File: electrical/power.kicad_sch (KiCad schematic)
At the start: 46 parts

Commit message: Added overview
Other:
- moved on the sheet: GTR20_CB
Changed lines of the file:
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@@
     (title "Power Distribution")
     (date "2024-02-12")
-    (rev "0.5")
+    (rev "0.9")
     (company "N877RV")
   )
@@
   (junction (at 127 40.64) (diameter 0) (color 0 0 0 0)
   )
-  (junction (at 175.26 137.16) (diameter 0) (color 0 0 0 0)
+  (junction (at 157.48 137.16) (diameter 0) (color 0 0 0 0)
   )
   (junction (at 123.19 222.25) (diameter 0) (color 0 0 0 0)
@@
     (stroke (width 0) (type default))
   )
-  (bus_entry (at 152.4 134.62) (size 2.54 2.54)
+  (bus_entry (at 134.62 134.62) (size 2.54 2.54)
     (stroke (width 0) (type default))
   )
@@
     (stroke (width 0) (type default))
   )
-  (wire (pts (xy 175.26 140.97) (xy 175.26 137.16))
+  (wire (pts (xy 157.48 140.97) (xy 157.48 137.16))
     (stroke (width 0) (type default))
   )
@@
     (stroke (width 0) (type default))
   )
-  (bus (pts (xy 134.62 124.46) (xy 134.62 143.51))
+  (bus (pts (xy 134.62 124.46) (xy 134.62 134.62))
+    (stroke (width 0) (type default))
+  )
+  (bus (pts (xy 134.62 134.62) (xy 134.62 143.51))
     (stroke (width 0) (type default))
   )
@@
     (stroke (width 0) (type default))
   )
-  (bus (pts (xy 152.4 127) (xy 152.4 134.62))
-    (stroke (width 0) (type default))
-  )
   (wire (pts (xy 127 60.96) (xy 133.35 60.96))
     (stroke (width 0) (type default))
@@
     (stroke (width 0) (type default))
   )
-  (wire (pts (xy 176.53 140.97) (xy 175.26 140.97))
+  (wire (pts (xy 158.75 140.97) (xy 157.48 140.97))
     (stroke (width 0) (type default))
   )
@@
     (stroke (width 0) (type default))
   )
-  (wire (pts (xy 154.94 137.16) (xy 157.48 137.16))
+  (wire (pts (xy 137.16 137.16) (xy 139.7 137.16))
     (stroke (width 0) (type default))
   )
@@
     (stroke (width 0) (type default))
   )
-  (wire (pts (xy 175.26 137.16) (xy 184.15 137.16))
+  (wire (pts (xy 157.48 137.16) (xy 166.37 137.16))
     (stroke (width 0) (type default))
   )
@@
     (effects (font (size 1.27 1.27)) (justify left))
   )
-  (hierarchical_label "GTR20_PWR" (shape output) (at 184.15 137.16 0) (fields_autoplaced)
+  (hierarchical_label "GTR20_PWR" (shape output) (at 166.37 137.16 0) (fields_autoplaced)
     (effects (font (size 1.27 1.27)) (justify left))
   )
@@
     (effects (font (size 1.27 1.27)) (justify left))
   )
-  (hierarchical_label "LEMO_PWR" (shape output) (at 184.15 140.97 0) (fields_autoplaced)
+  (hierarchical_label "LEMO_PWR" (shape output) (at 166.37 140.97 0) (fields_autoplaced)
     (effects (font (size 1.27 1.27)) (justify left))
   )
@@
     )
   )
-  (symbol (lib_id "Device:Fuse") (at 180.34 140.97 90) (unit 1)
-    (in_bom yes) (on_board yes) (dnp no)
-    (property "Reference" "LEMO_FS1" (at 180.34 137.16 90)
-      (effects (font (size 1.27 1.27)) hide)
-    )
-    (property "Value" "1" (at 180.34 138.43 90)
-      (effects (font (size 1.27 1.27)))
-    )
-    (property "Footprint" "" (at 180.34 142.748 90)
-      (effects (font (size 1.27 1.27)) hide)
-    )
-    (property "Datasheet" "~" (at 180.34 140.97 0)
+  (symbol (lib_id "Device:Fuse") (at 162.56 140.97 90) (unit 1)
+    (in_bom yes) (on_board yes) (dnp no)
+    (property "Reference" "LEMO_FS1" (at 162.56 137.16 90)
+      (effects (font (size 1.27 1.27)) hide)
+    )
+    (property "Value" "1" (at 162.56 138.43 90)
+      (effects (font (size 1.27 1.27)))
+    )
+    (property "Footprint" "" (at 162.56 142.748 90)
+      (effects (font (size 1.27 1.27)) hide)
+    )
+    (property "Datasheet" "~" (at 162.56 140.97 0)
       (effects (font (size 1.27 1.27)) hide)
     )
@@
     )
   )
-  (symbol (lib_id "flyerx:Circuit_Breaker") (at 166.37 134.62 0) (unit 1)
-    (in_bom yes) (on_board yes) (dnp no)
-    (property "Reference" "GTR20_CB" (at 166.37 132.08 0)
-      (effects (font (size 1.27 1.27)))
-    )
-    (property "Value" "3A" (at 166.37 137.16 0)
-      (effects (font (size 1.27 1.27)))
-    )
-    (property "Footprint" "" (at 166.37 134.62 0)
-      (effects (font (size 1.27 1.27)) hide)
-    )
-    (property "Datasheet" "" (at 166.37 134.62 0)
-      (effects (font (size 1.27 1.27)) hide)
-    )
+  (symbol (lib_id "flyerx:Circuit_Breaker") (at 148.59 134.62 0) (unit 1)
+    (in_bom yes) (on_board yes) (dnp no)
+    (property "Reference" "GTR20_CB" (at 148.59 132.08 0)
+      (effects (font (size 1.27 1.27)))
+    )
+    (property "Value" "3A" (at 148.59 137.16 0)
+      (effects (font (size 1.27 1.27)))
+    )
+    (property "Footprint" "" (at 148.59 134.62 0)
+      (effects (font (size 1.27 1.27)) hide)
+    )
+    (property "Datasheet" "" (at 148.59 134.62 0)
+      (effects (font (size 1.27 1.27)) hide)
+    )

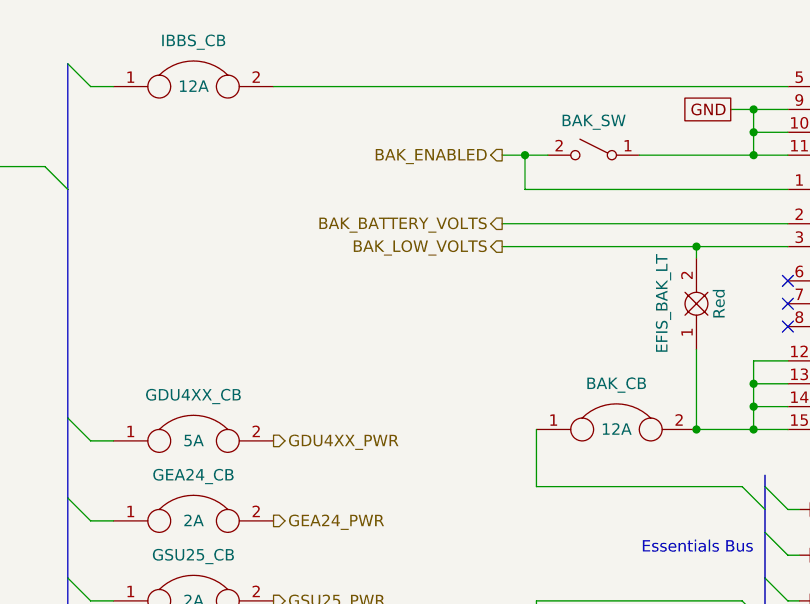
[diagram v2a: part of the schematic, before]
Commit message: Added V speeds to panel. Added note about backup power & circuit breakers. Changed backup battery circuit breaker size.
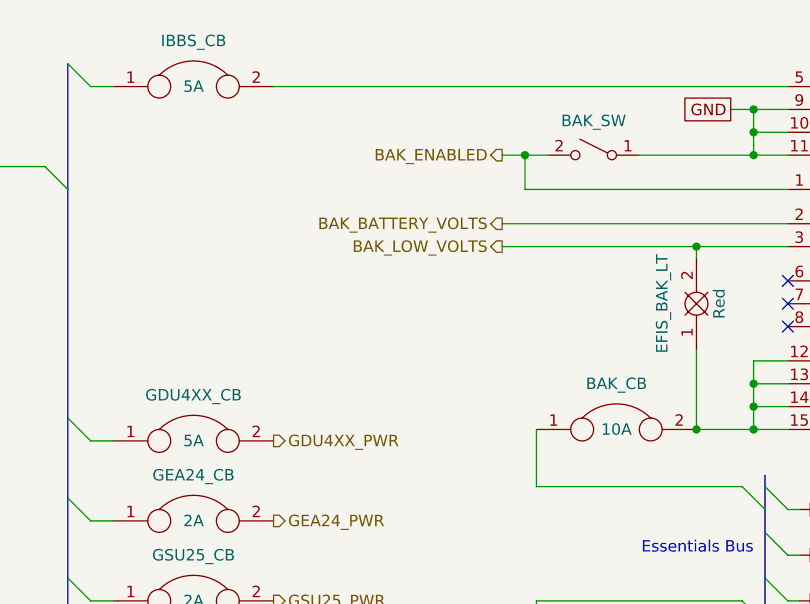
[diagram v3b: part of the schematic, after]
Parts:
- BAK_CB: value 12A -> 10A
- IBBS_CB: value 12A -> 5A
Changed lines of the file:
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@@
       (effects (font (size 1.27 1.27)))
     )
-    (property "Value" "12A" (at 71.12 22.86 0)
+    (property "Value" "5A" (at 71.12 22.86 0)
       (effects (font (size 1.27 1.27)))
     )
@@
       (effects (font (size 1.27 1.27)))
     )
-    (property "Value" "12A" (at 118.11 60.96 0)
-      (effects (font (size 1.27 1.27)))
-    )
+    (property "Value" "10A" (at 118.11 60.96 0)
+      (effects (font (size 1.27 1.27)))
+    )

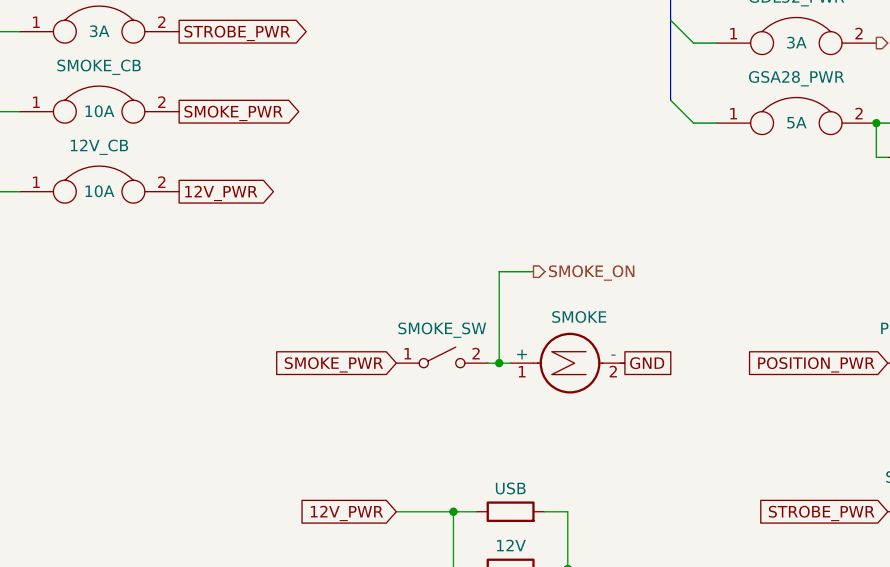
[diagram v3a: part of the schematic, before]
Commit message: Added smoke light to diagram
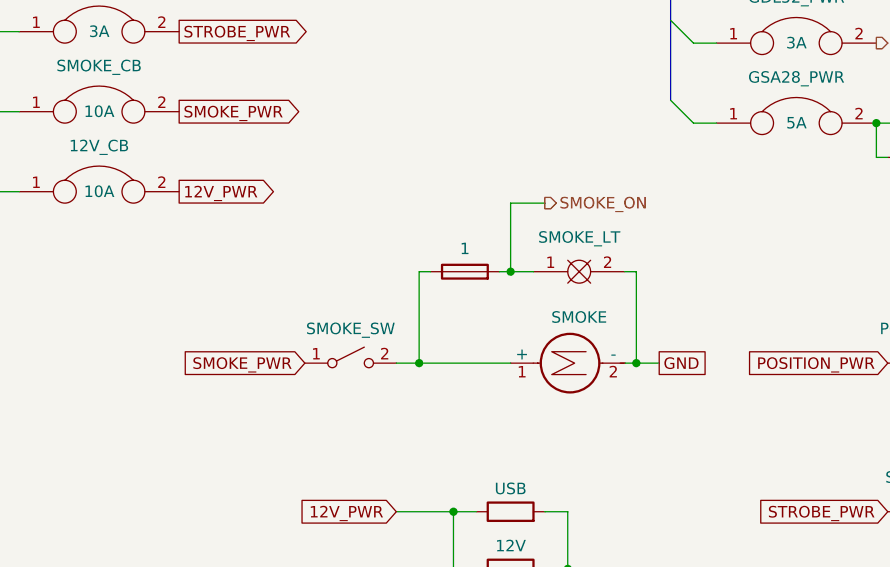
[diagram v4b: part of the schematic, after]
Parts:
- added SMOKE_LT: Clear, symbol FlyerX:Bulb
- added SMOKE_LT_FS: 1, symbol Device:Fuse
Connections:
- net GND: now also SMOKE_LT.2
- net SMOKE_ON: now also SMOKE_LT.1, SMOKE_LT_FS.2; no longer SMOKE.1 (+), SMOKE_SW.2 (B)
- new net: SMOKE.1 (+), SMOKE_LT_FS.1, SMOKE_SW.2 (B)
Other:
- moved on the sheet: SMOKE_SW
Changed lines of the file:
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@@
   (junction (at 172.72 199.39) (diameter 0) (color 0 0 0 0)
   )
-  (junction (at 115.57 199.39) (diameter 0) (color 0 0 0 0)
-  )
   (junction (at 157.48 172.72) (diameter 0) (color 0 0 0 0)
   )
@@
   (junction (at 133.35 27.94) (diameter 0) (color 0 0 0 0)
   )
+  (junction (at 106.68 199.39) (diameter 0) (color 0 0 0 0)
+  )
   (junction (at 127 60.96) (diameter 0) (color 0 0 0 0)
   )
   (junction (at 133.35 58.42) (diameter 0) (color 0 0 0 0)
   )
+  (junction (at 116.84 189.23) (diameter 0) (color 0 0 0 0)
+  )
   (junction (at 107.95 30.48) (diameter 0) (color 0 0 0 0)
+  )
+  (junction (at 130.81 199.39) (diameter 0) (color 0 0 0 0)
   )
   (junction (at 127 40.64) (diameter 0) (color 0 0 0 0)
@@
     (stroke (width 0) (type default))
   )
-  (wire (pts (xy 114.3 199.39) (xy 115.57 199.39))
+  (wire (pts (xy 104.14 199.39) (xy 106.68 199.39))
     (stroke (width 0) (type default))
   )
@@
     (stroke (width 0) (type default))
   )
+  (wire (pts (xy 133.35 199.39) (xy 130.81 199.39))
+    (stroke (width 0) (type default))
+  )
   (wire (pts (xy 137.16 146.05) (xy 139.7 146.05))
     (stroke (width 0) (type default))
@@
     (stroke (width 0) (type default))
   )
+  (wire (pts (xy 106.68 189.23) (xy 106.68 199.39))
+    (stroke (width 0) (type default))
+  )
   (wire (pts (xy 137.16 55.88) (xy 133.35 55.88))
     (stroke (width 0) (type default))
@@
     (stroke (width 0) (type default))
   )
-  (wire (pts (xy 119.38 189.23) (xy 115.57 189.23))
-    (stroke (width 0) (type default))
-  )
   (wire (pts (xy 105.41 30.48) (xy 107.95 30.48))
     (stroke (width 0) (type default))
@@
     (stroke (width 0) (type default))
   )
+  (wire (pts (xy 130.81 199.39) (xy 129.54 199.39))
+    (stroke (width 0) (type default))
+  )
   (wire (pts (xy 172.72 223.52) (xy 172.72 215.9))
     (stroke (width 0) (type default))
   )
-  (wire (pts (xy 115.57 189.23) (xy 115.57 199.39))
+  (wire (pts (xy 116.84 181.61) (xy 116.84 189.23))
     (stroke (width 0) (type default))
   )
@@
     (stroke (width 0) (type default))
   )
+  (wire (pts (xy 129.54 189.23) (xy 130.81 189.23))
+    (stroke (width 0) (type default))
+  )
   (wire (pts (xy 176.53 223.52) (xy 172.72 223.52))
     (stroke (width 0) (type default))
@@
     (stroke (width 0) (type default))
   )
+  (wire (pts (xy 116.84 189.23) (xy 119.38 189.23))
+    (stroke (width 0) (type default))
+  )
   (bus (pts (xy 57.15 160.02) (xy 57.15 168.91))
     (stroke (width 0) (type default))
@@
     (stroke (width 0) (type default))
   )
+  (wire (pts (xy 106.68 189.23) (xy 107.95 189.23))
+    (stroke (width 0) (type default))
+  )
   (wire (pts (xy 120.65 30.48) (xy 133.35 30.48))
     (stroke (width 0) (type default))
@@
     (stroke (width 0) (type default))
   )
-  (wire (pts (xy 115.57 199.39) (xy 116.84 199.39))
-    (stroke (width 0) (type default))
-  )
   (bus (pts (xy 57.15 95.25) (xy 57.15 105.41))
     (stroke (width 0) (type default))
@@
     (stroke (width 0) (type default))
   )
+  (wire (pts (xy 115.57 189.23) (xy 116.84 189.23))
+    (stroke (width 0) (type default))
+  )
   (wire (pts (xy 157.48 154.94) (xy 160.02 154.94))
     (stroke (width 0) (type default))
@@
     (stroke (width 0) (type default))
   )
+  (wire (pts (xy 130.81 189.23) (xy 130.81 199.39))
+    (stroke (width 0) (type default))
+  )
   (bus (pts (xy 57.15 68.58) (xy 57.15 77.47))
     (stroke (width 0) (type default))
@@
     (stroke (width 0) (type default))
   )
+  (wire (pts (xy 120.65 181.61) (xy 116.84 181.61))
+    (stroke (width 0) (type default))
+  )
   (wire (pts (xy 172.72 215.9) (xy 176.53 215.9))
     (stroke (width 0) (type default))
   )
   (wire (pts (xy 109.22 67.31) (xy 132.08 67.31))
+    (stroke (width 0) (type default))
+  )
+  (wire (pts (xy 106.68 199.39) (xy 116.84 199.39))
     (stroke (width 0) (type default))
   )
@@
     )
   )
-  (global_label "SMOKE_PWR" (shape input) (at 104.14 199.39 180) (fields_autoplaced)
+  (global_label "SMOKE_PWR" (shape input) (at 93.98 199.39 180) (fields_autoplaced)
     (effects (font (size 1.27 1.27)) (justify right))
-    (property "Intersheetrefs" "${INTERSHEET_REFS}" (at 89.7854 199.39 0)
+    (property "Intersheetrefs" "${INTERSHEET_REFS}" (at 79.6254 199.39 0)
       (effects (font (size 1.27 1.27)) (justify right) hide)
     )
@@
     )
   )
-  (global_label "GND" (shape passive) (at 129.54 199.39 0) (fields_autoplaced)
-    (effects (font (size 1.27 1.27)) (justify left))
-    (property "Intersheetrefs" "${INTERSHEET_REFS}" (at 135.2844 199.39 0)
+  (global_label "GND" (shape passive) (at 133.35 199.39 0) (fields_autoplaced)
+    (effects (font (size 1.27 1.27)) (justify left))
+    (property "Intersheetrefs" "${INTERSHEET_REFS}" (at 139.0944 199.39 0)
       (effects (font (size 1.27 1.27)) (justify left) hide)
     )
@@
     (effects (font (size 1.27 1.27)) (justify left))
   )
-  (hierarchical_label "SMOKE_ON" (shape output) (at 119.38 189.23 0) (fields_autoplaced)
+  (hierarchical_label "SMOKE_ON" (shape output) (at 120.65 181.61 0) (fields_autoplaced)
     (effects (font (size 1.27 1.27)) (justify left))
   )
@@
     )
   )
-  (symbol (lib_id "Switch:SW_SPST") (at 109.22 199.39 0) (unit 1)
-    (in_bom yes) (on_board yes) (dnp no)
-    (property "Reference" "SMOKE_SW" (at 109.22 195.58 0)
-      (effects (font (size 1.27 1.27)))
-    )
-    (property "Value" "~" (at 109.22 195.58 0)
-      (effects (font (size 1.27 1.27)))
-    )
-    (property "Footprint" "" (at 109.22 199.39 0)
-      (effects (font (size 1.27 1.27)) hide)
-    )
-    (property "Datasheet" "~" (at 109.22 199.39 0)
+  (symbol (lib_id "Switch:SW_SPST") (at 99.06 199.39 0) (unit 1)
+    (in_bom yes) (on_board yes) (dnp no)
+    (property "Reference" "SMOKE_SW" (at 99.06 195.58 0)
+      (effects (font (size 1.27 1.27)))
+    )
+    (property "Value" "~" (at 99.06 195.58 0)
+      (effects (font (size 1.27 1.27)))
+    )
+    (property "Footprint" "" (at 99.06 199.39 0)
+      (effects (font (size 1.27 1.27)) hide)
+    )
+    (property "Datasheet" "~" (at 99.06 199.39 0)
       (effects (font (size 1.27 1.27)) hide)
     )
@@
         )
       )
+    )
+  )
+  (symbol (lib_id "FlyerX:Bulb") (at 123.19 187.96 0) (unit 1)
+    (in_bom yes) (on_board yes) (dnp no)
+    (property "Reference" "SMOKE_LT" (at 124.46 185.42 0)
+      (effects (font (size 1.27 1.27)))
+    )
+    (property "Value" "Clear" (at 124.46 191.77 0)
+      (effects (font (size 1.27 1.27)) hide)
+    )
+    (property "Footprint" "" (at 124.46 186.69 0)
+      (effects (font (size 1.27 1.27)) hide)
+    )
+    (property "Datasheet" "" (at 124.46 186.69 0)
+      (effects (font (size 1.27 1.27)) hide)
+    )
+    (pin "1")
+    (pin "2")
+    (instances
+      (project "electrical"
+        (path "/e8ec215a-dbe2-4eba-a577-e50a0a128049/2852c073-fbc9-4469-a6bf-ba3e911c7f5a"
+          (reference "SMOKE_LT") (unit 1)
+        )
+      )
+    )
+  )
+  (symbol (lib_id "Device:Fuse") (at 111.76 189.23 90) (unit 1)
+    (in_bom yes) (on_board yes) (dnp no)
+    (property "Reference" "SMOKE_LT_FS" (at 111.76 185.42 90)
+      (effects (font (size 1.27 1.27)) hide)
+    )
+    (property "Value" "1" (at 111.76 186.69 90)
+      (effects (font (size 1.27 1.27)))
+    )
+    (property "Footprint" "" (at 111.76 191.008 90)
+      (effects (font (size 1.27 1.27)) hide)
+    )
+    (property "Datasheet" "~" (at 111.76 189.23 0)
+      (effects (font (size 1.27 1.27)) hide)
+    )
+    (pin "1")
+    (pin "2")
+    (instances
+      (project "electrical"
+        (path "/e8ec215a-dbe2-4eba-a577-e50a0a128049/2852c073-fbc9-4469-a6bf-ba3e911c7f5a"
+          (reference "SMOKE_LT_FS") (unit 1)
+        )
+      )
